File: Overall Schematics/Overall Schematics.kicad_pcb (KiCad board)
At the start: 2 copper layers, 152.4 x 167.9 mm, 32 parts, among them J1 WattMeter1_Output, J2 WattMeter2_Output, J3 Intel_Buck_Converter_Input, M1 Stepper_Motor_bipolar, M10 Motor_Servo, M11 Stepper_Motor_bipolar, M12 Motor_Servo, M2 Stepper_Motor_bipolar, M3 LinActuator12V, M4 LinActuator12V, M5 LinActuator12V, M6 Motor_DC, M7 Motor_DC, M8 Motor_DC, M9 Motor_DC, U1 Teensy4.1, U10 VNH52019, U11 ServoDriver, U12 36v4SMD, U13 D24V22F5, U2 36v4SMD, U3 36v4SMD, U4 VNH52019, U5 VNH52019, U6 VNH52019, U7 VNH52019, U8 VNH52019, U9 VNH52019

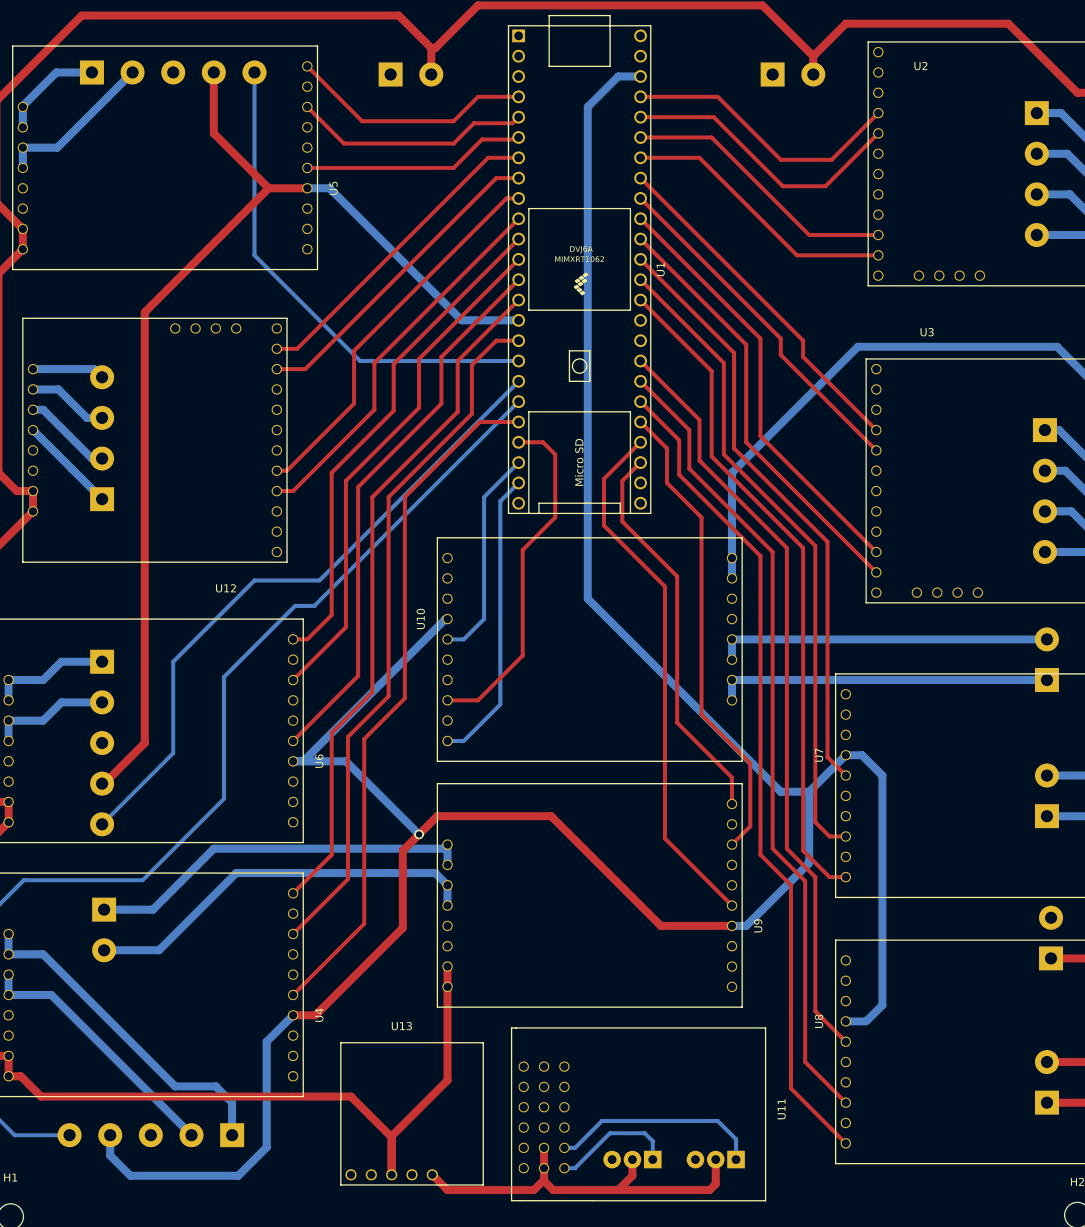
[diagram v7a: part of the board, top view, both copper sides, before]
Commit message: added the silkscreens
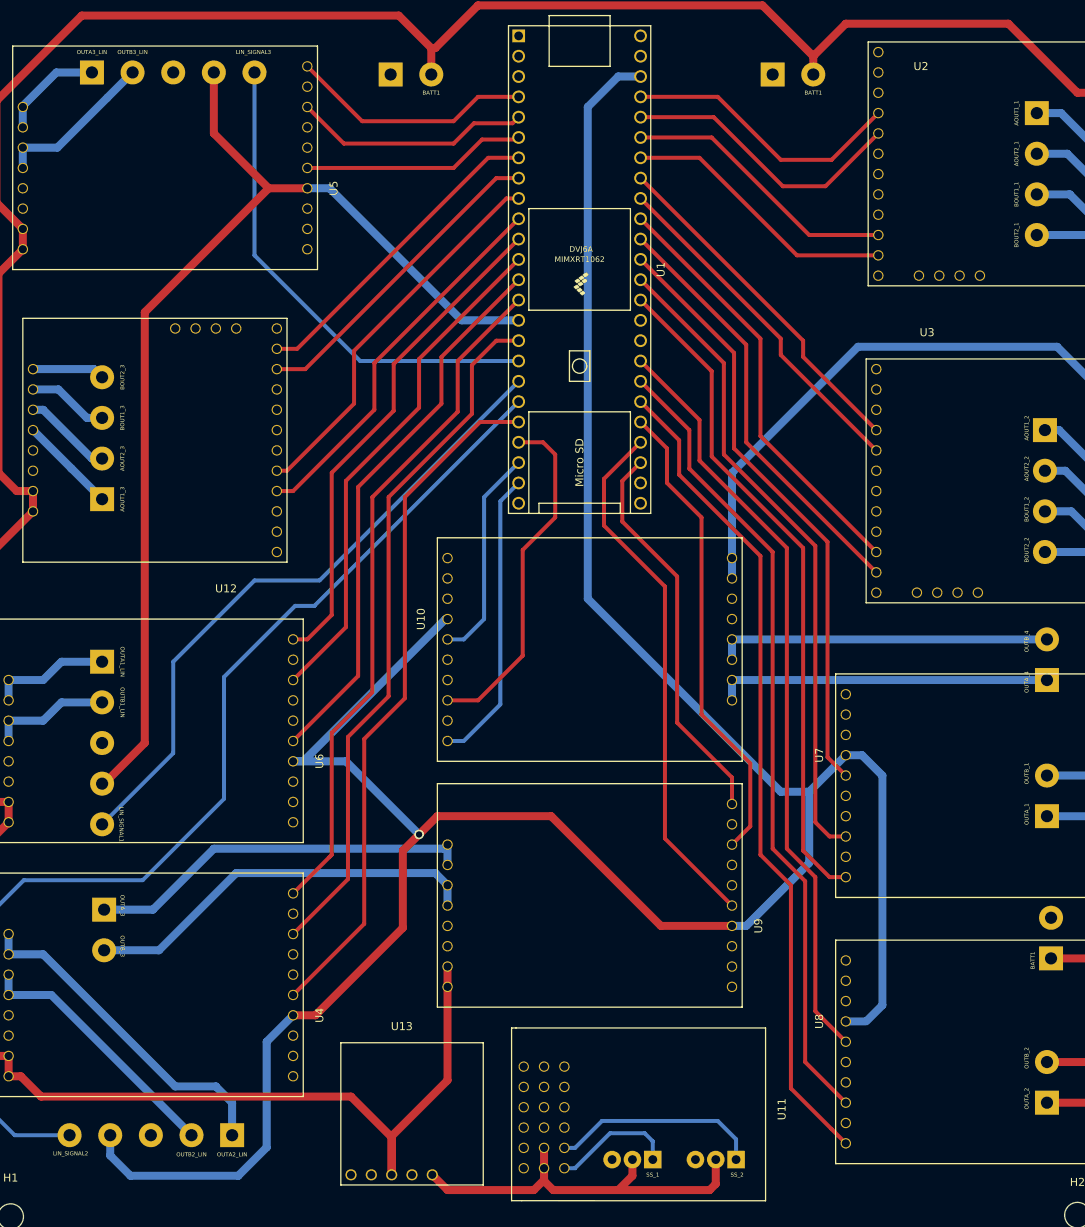
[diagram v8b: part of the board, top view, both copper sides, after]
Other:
- board text added: "AOUT1_1"
- board text added: "AOUT1_2"
- board text added: "AOUT1_3"
- board text added: "AOUT2_1"
- board text added: "AOUT2_2"
- board text added: "AOUT2_3"
- board text added: "BATT1"
- board text added: "BOUT1_1"
- board text added: "BOUT1_2"
- board text added: "BOUT1_3"
- board text added: "BOUT2_1"
- board text added: "BOUT2_2"
- board text added: "BOUT2_3"
- board text added: "LIN_SIGNAL1"
- board text added: "LIN_SIGNAL2"
- board text added: "LIN_SIGNAL3"
- board text added: "OUTA1_LIN"
- board text added: "OUTA2_LIN"
- board text added: "OUTA3_LIN"
- board text added: "OUTA_1"
- board text added: "OUTA_2"
- board text added: "OUTA_3"
- board text added: "OUTA_4"
- board text added: "OUTB1_LIN"
- board text added: "OUTB2_LIN"
- board text added: "OUTB3_LIN"
- board text added: "OUTB_1"
- board text added: "OUTB_2"
- board text added: "OUTB_3"
- board text added: "OUTB_4"
- board text added: "SS_1"
- board text added: "SS_2"
